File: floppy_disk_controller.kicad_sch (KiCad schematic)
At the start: 60 parts, among them J1 Conn_02x18_Odd_Even, U15 L78L05_TO92

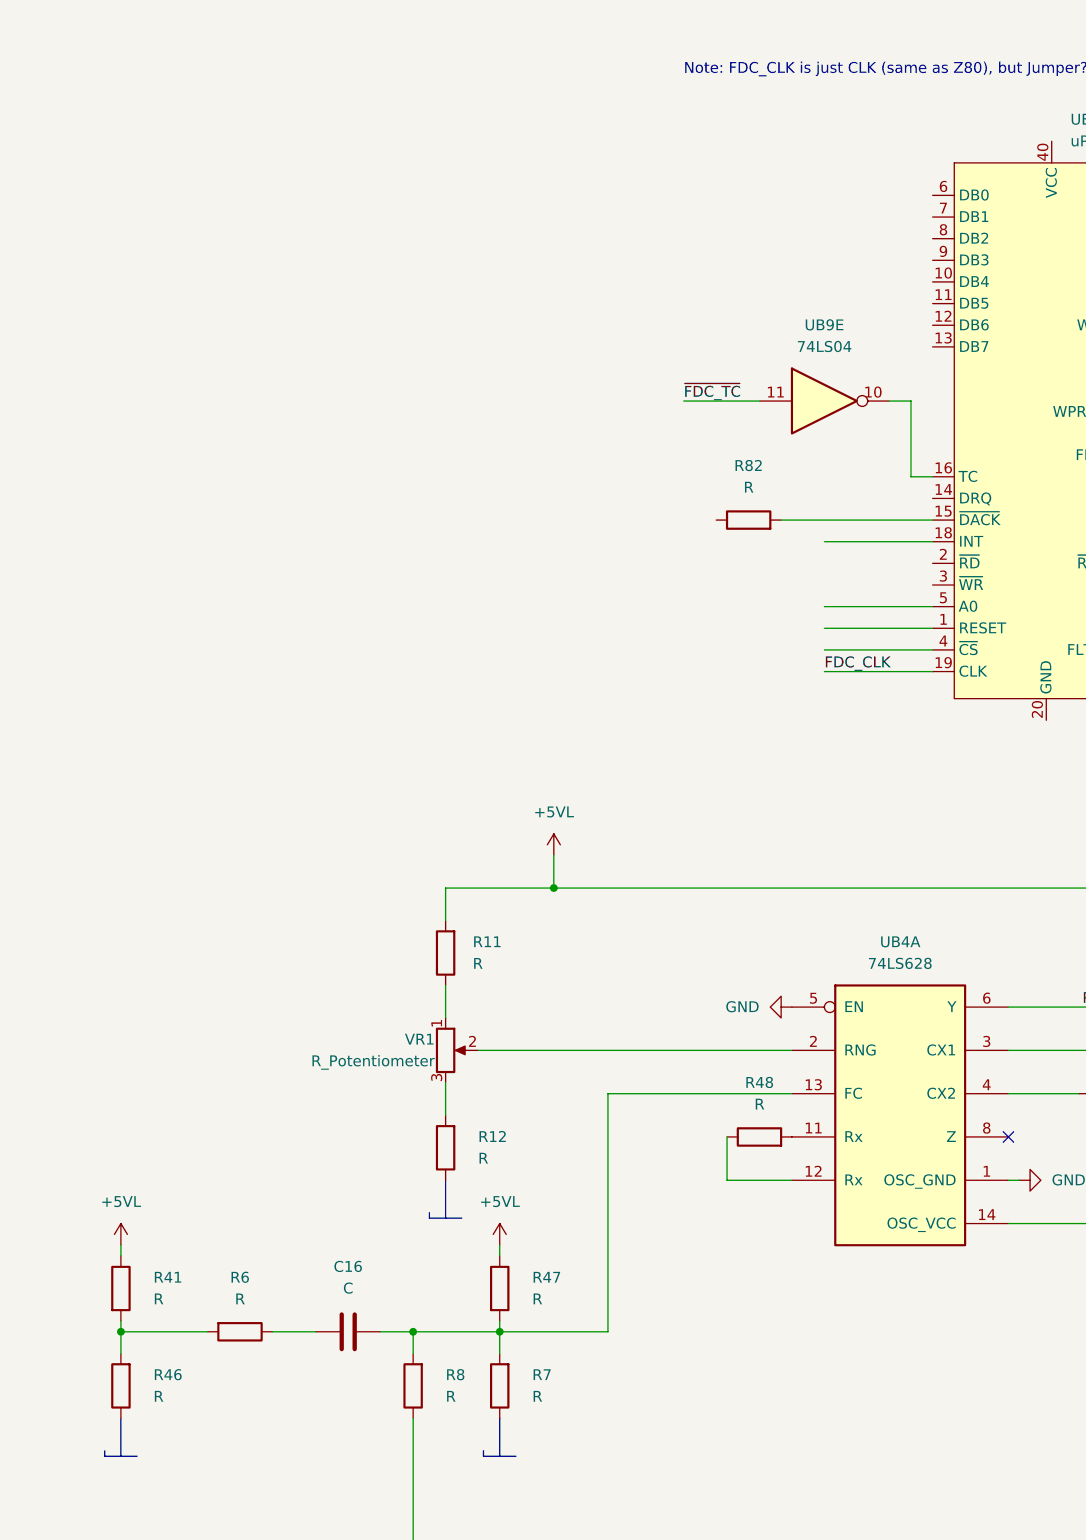
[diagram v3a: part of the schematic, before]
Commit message: Renamed conflicting resistors in FDC
R1xx are randomly assigned just to avoid conflicts with following commit
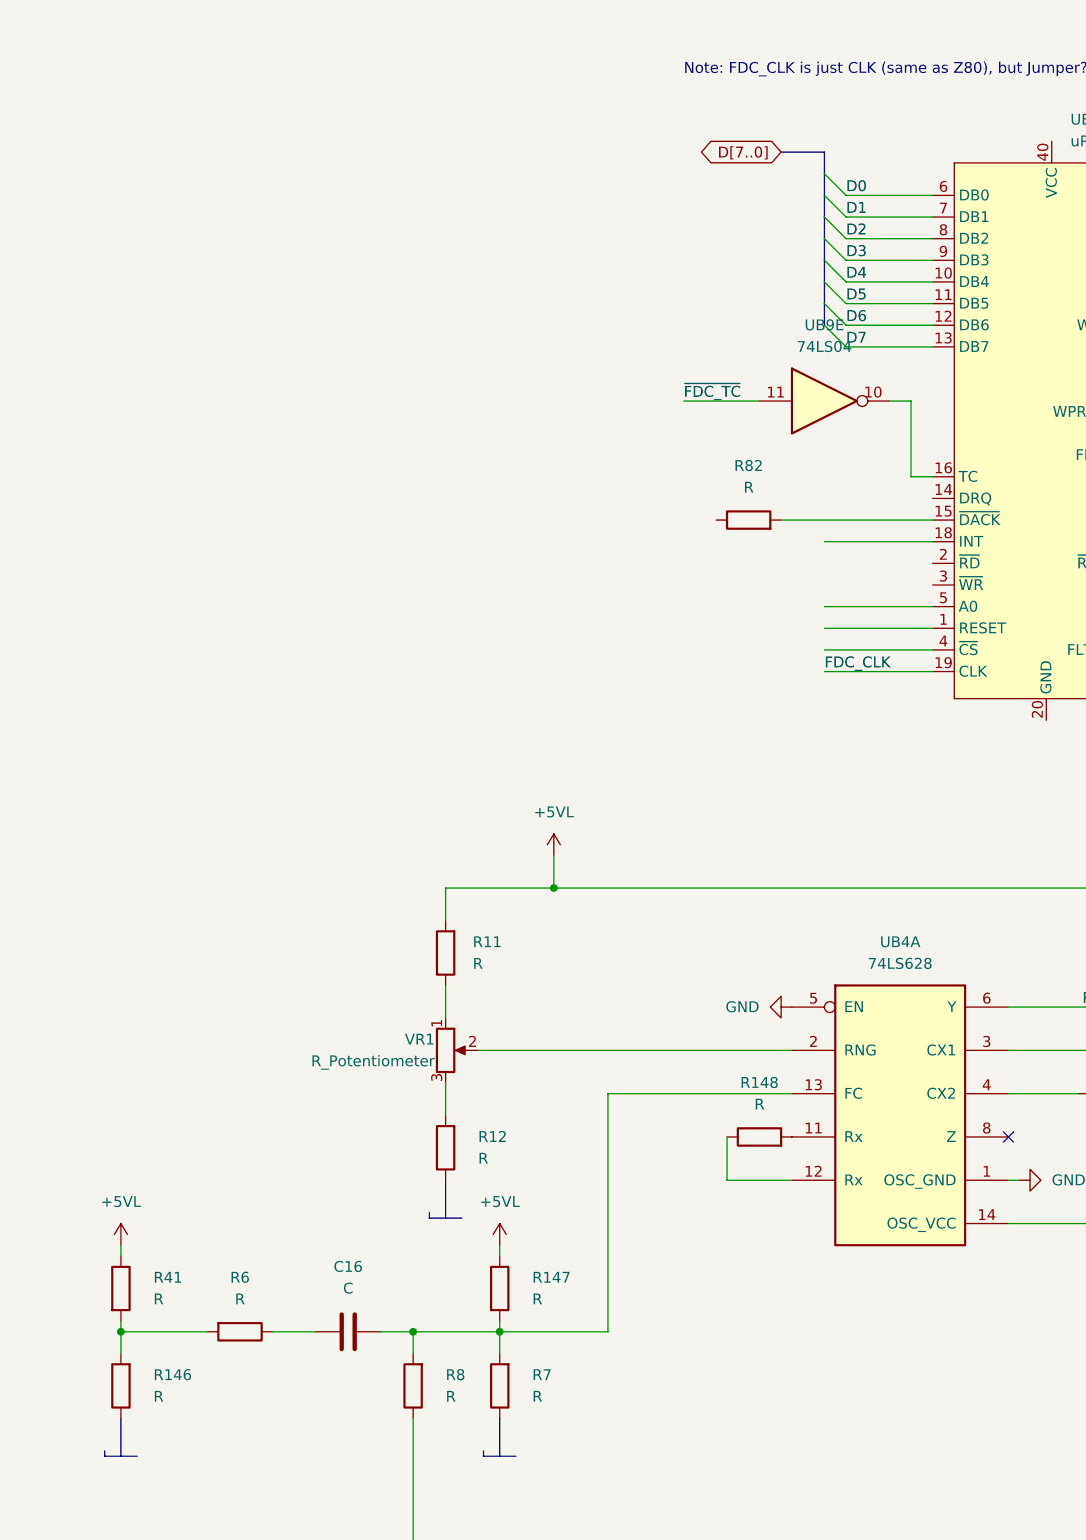
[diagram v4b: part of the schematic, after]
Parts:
- renumbered R46 to R146, R47 to R147, R48 to R148
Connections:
- net D4: now reaches UE2.10 (DB4)
- net D5: now reaches UE2.11 (DB5)
- net D6: now reaches UE2.12 (DB6)
- net D7: now reaches UE2.13 (DB7)
- net D0: now reaches UE2.6 (DB0)
- net D1: now reaches UE2.7 (DB1)
- net D2: now reaches UE2.8 (DB2)
- net D3: now reaches UE2.9 (DB3)

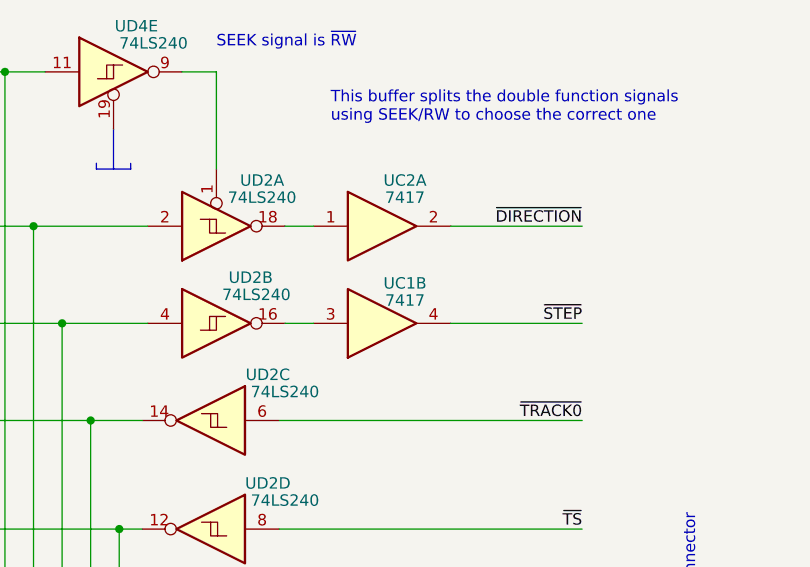
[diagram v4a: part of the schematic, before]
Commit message: fdc: wrong component removed
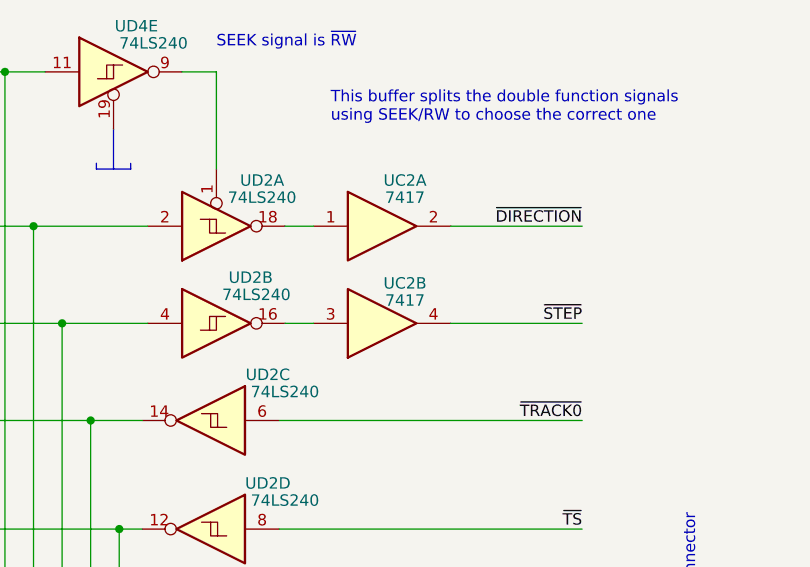
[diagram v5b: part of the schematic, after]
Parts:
- renumbered UC1 to UC2
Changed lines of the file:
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@@
 		(on_board yes)
 		(dnp no)
-		(property "Reference" "UC1"
+		(property "Reference" "UC2"
 			(at 359.41 161.925 0)
 			(effects
@@
 			(project "ceda"
 				(path "/12a6dbe3-008d-4c5b-88f6-9f1c816060be/30cc577a-62cc-4eb0-beb7-81a864bc3256"
-					(reference "UC1")
+					(reference "UC2")
 					(unit 2)
 				)

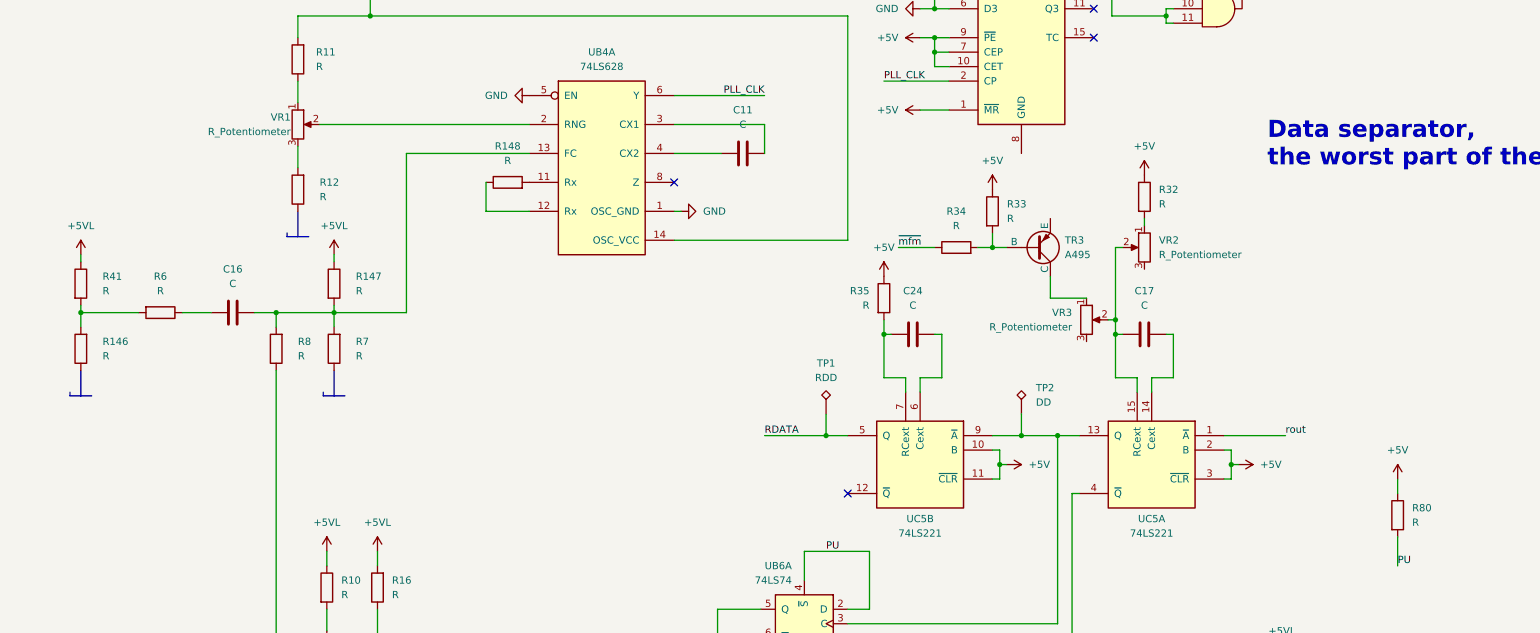
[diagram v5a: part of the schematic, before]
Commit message: pcb: added and placed almost all components
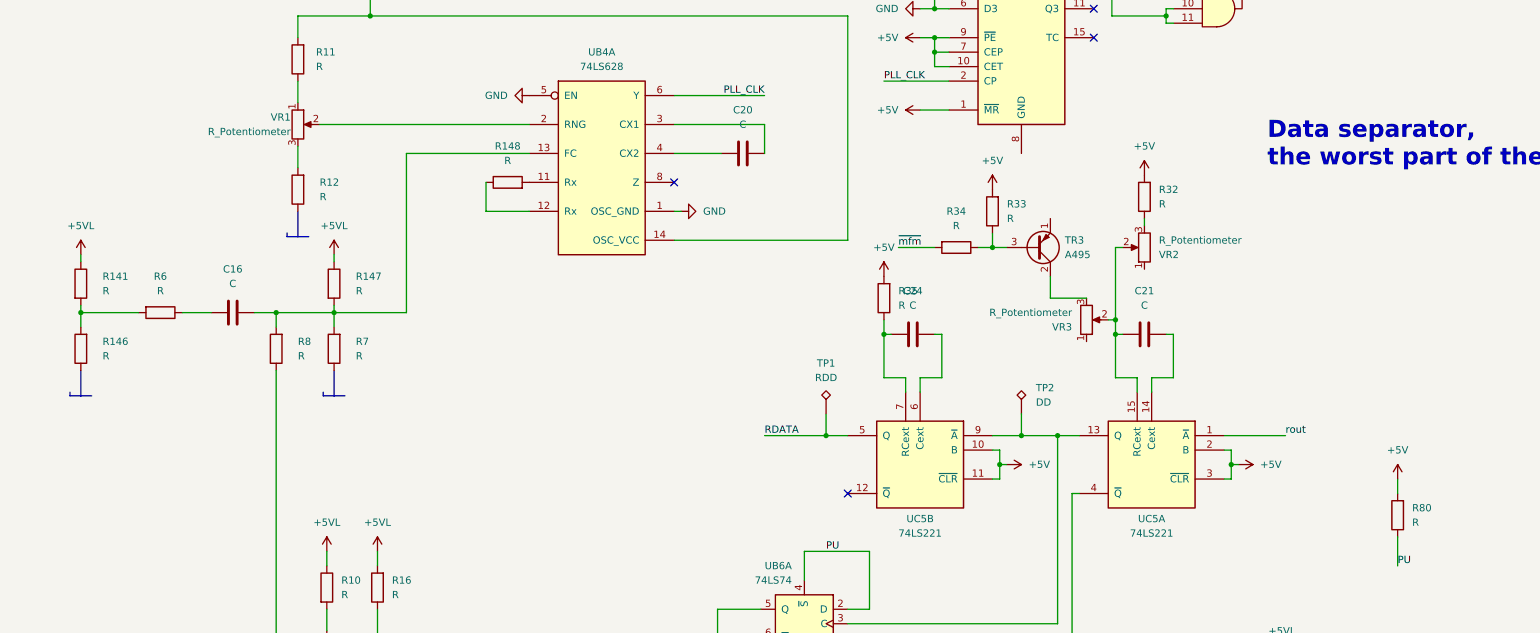
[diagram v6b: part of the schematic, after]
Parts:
- C16, C2, C24, C7: footprint (none) -> Capacitor_THT:C_Disc_D4.3mm_W1.9mm_P5.00mm
- C20: renamed from C11; footprint (none) -> Capacitor_THT:C_Disc_D4.3mm_W1.9mm_P5.00mm
- C21: renamed from C17; footprint (none) -> Capacitor_THT:C_Disc_D4.3mm_W1.9mm_P5.00mm
- D1, D4: footprint (none) -> Diode_THT:D_A-405_P5.08mm_Vertical_KathodeUp
- J1: footprint (none) -> Connector_IDC:IDC-Header_2x25_P2.54mm_Vertical
- JP1: footprint (none) -> Connector_PinHeader_2.54mm:PinHeader_2x01_P2.54mm_Vertical
- R10, R11, R12, R13, R14, R146, R147, R148, R15, R16, R32, R33, R34, R35, R5, R6, R7, R8, R80, R82: footprint (none) -> Resistor_THT:R_Axial_DIN0204_L3.6mm_D1.6mm_P5.08mm_Vertical
- R141: renamed from R41; footprint (none) -> Resistor_THT:R_Axial_DIN0204_L3.6mm_D1.6mm_P5.08mm_Vertical
- TP1, TP2, TP3: footprint (none) -> TestPoint:TestPoint_Plated_Hole_D2.0mm
- TR1, TR2: footprint (none) -> Package_TO_SOT_THT:TO-92_Inline_Wide
- TR3: footprint (none) -> Package_TO_SOT_THT:TO-92_Inline_Wide; symbol Simulation_SPICE:PNP -> Transistor_BJT:Q_PNP_ECB
- U15: footprint Package_TO_SOT_THT:TO-92_Inline -> Package_TO_SOT_THT:TO-92_Inline_Wide
- VR1, VR2, VR3: footprint (none) -> Ceda:Round_Trimmer
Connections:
- net +5V: now also R32.2, R33.2, R35.2, R80.2; no longer R32.1, R33.1, R35.1, R80.1
- net PU: now also R80.1; no longer R80.2
- net ~{mfm}: now also R34.2; no longer R34.1
- net at TR3.1 (E): no longer VR3.1
- net at TR3.3 (B): now also R33.1, R34.1
- net at VR2.1: no longer R32.2
- net at C24.1, UC5.7 (RCext): now also R35.1; no longer R35.2
- net at VR2.3: now also R32.1
- net at VR3.3: now also TR3.2 (C)
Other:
- moved on the sheet: R32, R33, R34, R35, R80, VR2

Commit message: sch: fixed fdc connections according to actual measurements on pcb
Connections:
- net +5V: now also R82.1, TR3.1 (E), UB7.16 (VCC), UE2.40 (VCC)
- net GND: now also R12.1, R14.2, R146.1, R5.1, R7.1, U15.2 (GND), UB3.15 (E), UB5.7 (GND), UB7.8 (GND), UD4.1, UD4.19, UE2.20 (GND)
- no-connect marks 14 -> 16
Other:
- moved on the sheet: UB9E

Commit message: pcb: added all the connector, 99% routed
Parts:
- added C104, C8: C, Capacitor_THT:C_Disc_D4.3mm_W1.9mm_P5.00mm, symbol Device:C
- added C6, C7778: C_Polarized, Capacitor_THT:CP_Radial_D5.0mm_P2.50mm, symbol Device:C_Polarized
- added RM3: 150, Resistor_THT:R_Array_SIP9, symbol Device:R_Network08
- TR1: symbol Simulation_SPICE:NPN -> Transistor_BJT:Q_NPN_ECB
- TR2: symbol Simulation_SPICE:PNP -> Transistor_BJT:Q_PNP_ECB
- renumbered C7 to C10, C2 to C9, R146 to R1, R141 to R2, R148 to R30
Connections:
- net +5V: now also UB6.10 (~{S}), UB6.13 (~{R})
- net +5VL: now also R10.2, R11.1, R16.1, C7778.1, C8.1; no longer R10.1, R11.2, R16.2, UB6.10 (~{S}), UB6.13 (~{R})
- net GND: now also R12.2, C104.2, C6.2, C7778.2, C8.2; no longer R12.1
- net ~{FLT}: now also RM3.7 (R6)
- net ~{INDEX}: now also RM3.6 (R5)
- net ~{RD_DATA}: now also RM3.2 (R1)
- net ~{READY}: now also RM3.3 (R2)
- net ~{TRACK0}: now also RM3.5 (R4)
- net ~{TS}: now also RM3.8 (R7)
- net ~{WRITE_PROTECT}: now also RM3.9 (R8)
- net at VR1.3: now also R11.2; no longer R12.2
- net at TR1.1 (E): now also R5.2; no longer D1.1 (K)
- net at C9.1, R14.1: now also R13.2, TR1.3 (B); no longer R13.1, TR1.2 (B)
- net at C9.2, UB5.5 (Q), UF14.2: now also R13.1; no longer R13.2
- net at TR2.1 (E): now also R10.1; no longer D4.2 (A)
- net at TR2.3 (B): now also C10.1, R15.1, R16.2; no longer R10.2
- net at U15.3 (VI): now also C104.1, C6.1
- net at UB4.11 (Rx): now also R30.1; no longer R30.2
- net at UB4.12 (Rx): now also R30.2; no longer R30.1
- net at VR1.1: now also R12.1; no longer R11.1
- net RESET: now reaches UE2.1 (RESET)
- net FDC_INT: now reaches UE2.18 (INT)
- net ~{RD}: now reaches UE2.2 (~{RD})
- net ~{WR}: now reaches UE2.3 (~{WR})
- net ~{FDC_CS}: now reaches UE2.4 (~{CS})
- net A0: now reaches UE2.5 (A0)
- net at C10.2, UB5.8 (~{Q}): now also R15.2; no longer R15.1
- new net: D1.1 (K), TR1.2 (C)
- new net: D4.2 (A), TR2.2 (C)
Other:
- moved on the sheet: R10, R11, R12, R13, R15, R16, R30, R82
